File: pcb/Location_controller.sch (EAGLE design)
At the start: 55 parts, among them IC1 LIS302DL

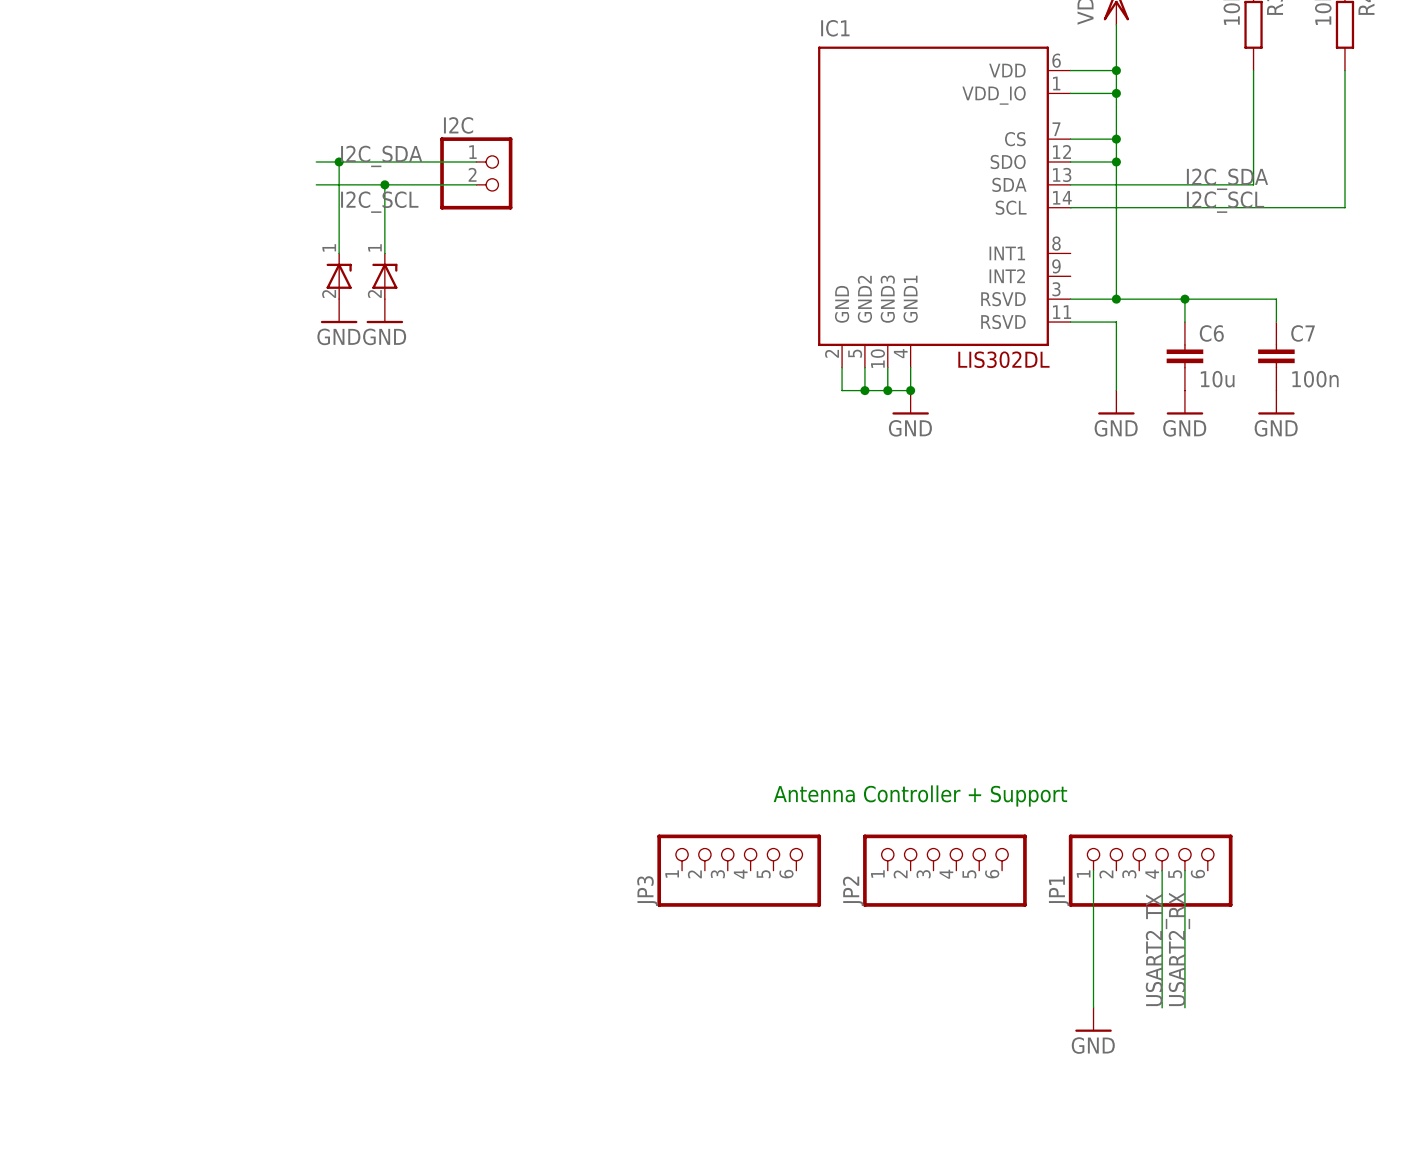
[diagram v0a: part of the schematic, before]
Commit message: Add TVS for I2C and USART connections
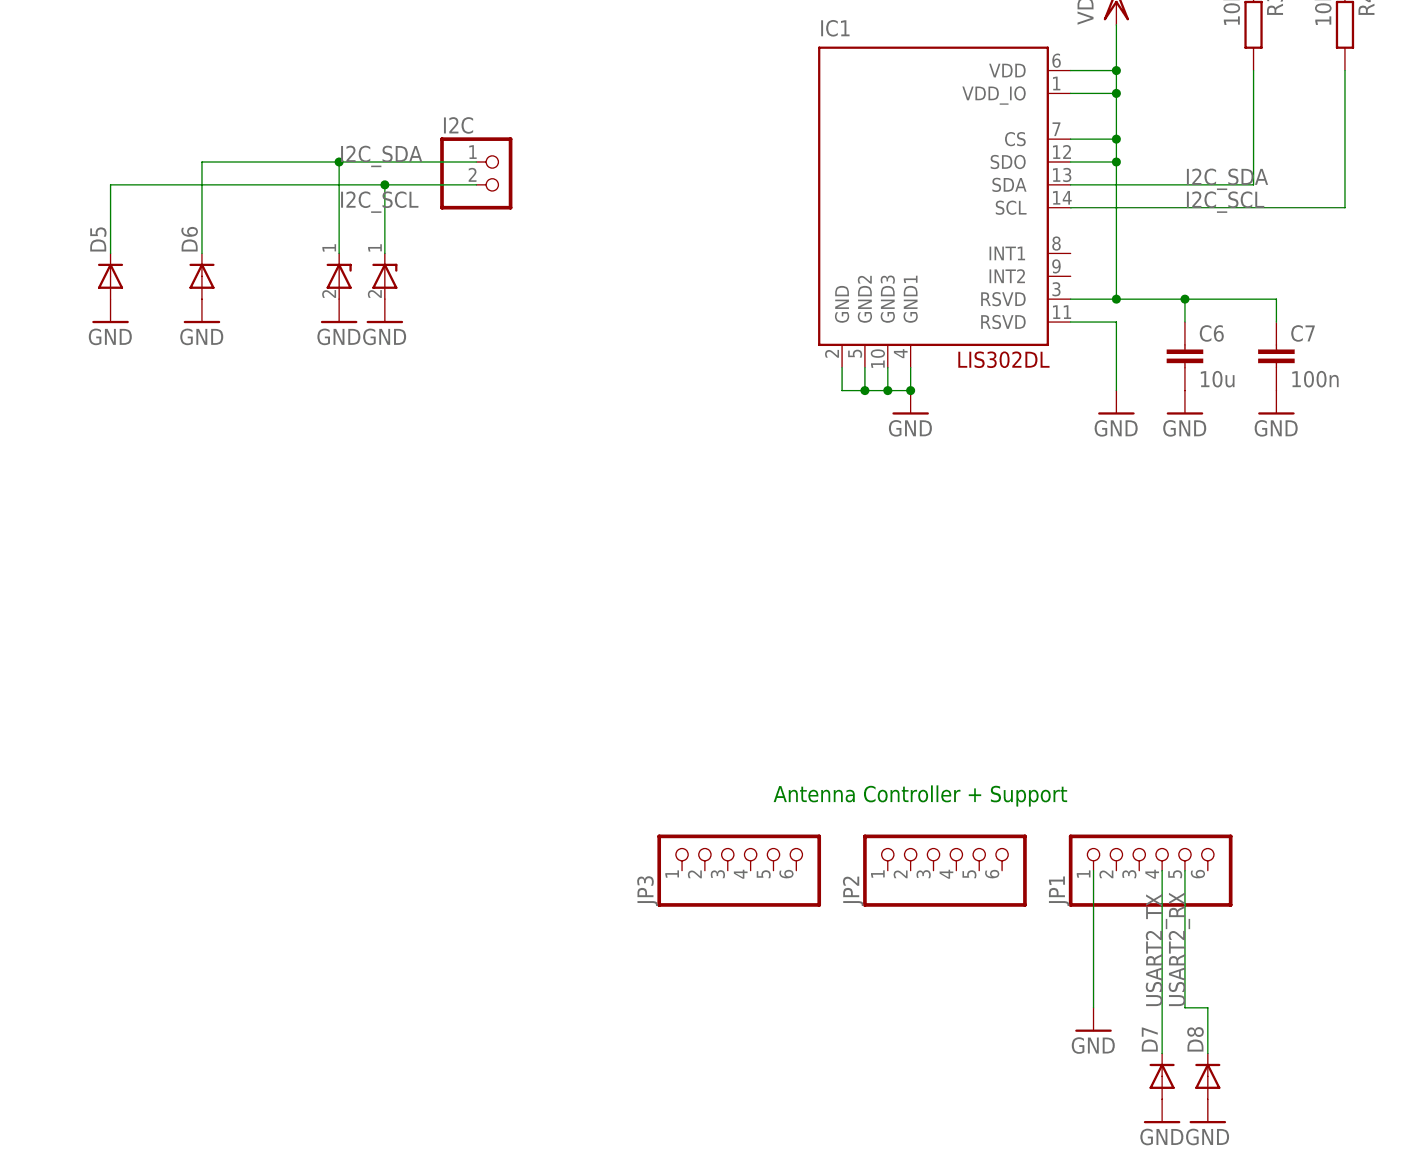
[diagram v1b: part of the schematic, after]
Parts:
- added D5, D6, D7, D8: (no value), diode:DIODE-SOD523
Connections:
- net GND: now also D5.A, D6.A, D7.A, D8.A
- net I2C_SCL: now also D5.C
- net I2C_SDA: now also D6.C
- net USART2_RX: now also D8.C
- net USART2_TX: now also D7.C
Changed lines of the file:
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@@
 <?xml version="1.0" encoding="utf-8"?>
 <!DOCTYPE eagle SYSTEM "eagle.dtd">
-<eagle version="6.4">
+<eagle version="6.5.0">
 <drawing>
 <settings>
@@
 <part name="D3" library="stm32f4" deviceset="ZDIODE" device=""/>
 <part name="GND25" library="supply1" deviceset="GND" device=""/>
+<part name="D5" library="diode" deviceset="DIODE-" device="SOD523"/>
+<part name="D6" library="diode" deviceset="DIODE-" device="SOD523"/>
+<part name="GND27" library="supply1" deviceset="GND" device=""/>
+<part name="GND28" library="supply1" deviceset="GND" device=""/>
+<part name="D7" library="diode" deviceset="DIODE-" device="SOD523"/>
+<part name="D8" library="diode" deviceset="DIODE-" device="SOD523"/>
+<part name="GND29" library="supply1" deviceset="GND" device=""/>
+<part name="GND30" library="supply1" deviceset="GND" device=""/>
 </parts>
 <sheets>
@@
 <instance part="D3" gate="G$1" x="78.74" y="-60.96" rot="R90"/>
 <instance part="GND25" gate="1" x="78.74" y="-88.9"/>
+<instance part="D5" gate="G$1" x="-149.86" y="2.54" rot="R90"/>
+<instance part="D6" gate="G$1" x="-139.7" y="2.54" rot="R90"/>
+<instance part="GND27" gate="1" x="-139.7" y="-2.54"/>
+<instance part="GND28" gate="1" x="-149.86" y="-2.54"/>
+<instance part="D7" gate="G$1" x="-33.02" y="-86.36" rot="R90"/>
+<instance part="D8" gate="G$1" x="-27.94" y="-86.36" rot="R90"/>
+<instance part="GND29" gate="1" x="-33.02" y="-91.44"/>
+<instance part="GND30" gate="1" x="-27.94" y="-91.44"/>
 </instances>
 <busses>
@@
 <wire x1="78.74" y1="-86.36" x2="78.74" y2="-63.5" width="0.1524" layer="91"/>
 </segment>
+<segment>
+<pinref part="D6" gate="G$1" pin="A"/>
+<pinref part="GND27" gate="1" pin="GND"/>
+</segment>
+<segment>
+<pinref part="D5" gate="G$1" pin="A"/>
+<pinref part="GND28" gate="1" pin="GND"/>
+</segment>
+<segment>
+<pinref part="D7" gate="G$1" pin="A"/>
+<pinref part="GND29" gate="1" pin="GND"/>
+</segment>
+<segment>
+<pinref part="D8" gate="G$1" pin="A"/>
+<pinref part="GND30" gate="1" pin="GND"/>
+</segment>
 </net>
 <net name="N$1" class="0">
@@
 <label x="-124.46" y="10.16" size="1.778" layer="95"/>
 <pinref part="D2" gate="G$1" pin="P1"/>
-<wire x1="-119.38" y1="12.7" x2="-127" y2="12.7" width="0.1524" layer="91"/>
 <wire x1="-119.38" y1="5.08" x2="-119.38" y2="12.7" width="0.1524" layer="91"/>
 <junction x="-119.38" y="12.7"/>
+<pinref part="D5" gate="G$1" pin="C"/>
+<wire x1="-119.38" y1="12.7" x2="-149.86" y2="12.7" width="0.1524" layer="91"/>
+<wire x1="-149.86" y1="12.7" x2="-149.86" y2="5.08" width="0.1524" layer="91"/>
 </segment>
 </net>
@@
 <label x="-124.46" y="15.24" size="1.778" layer="95"/>
 <pinref part="D1" gate="G$1" pin="P1"/>
-<wire x1="-124.46" y1="15.24" x2="-127" y2="15.24" width="0.1524" layer="91"/>
 <wire x1="-124.46" y1="5.08" x2="-124.46" y2="15.24" width="0.1524" layer="91"/>
 <junction x="-124.46" y="15.24"/>
+<pinref part="D6" gate="G$1" pin="C"/>
+<wire x1="-124.46" y1="15.24" x2="-139.7" y2="15.24" width="0.1524" layer="91"/>
+<wire x1="-139.7" y1="15.24" x2="-139.7" y2="5.08" width="0.1524" layer="91"/>
 </segment>
 </net>
@@
 <segment>
 <pinref part="JP1" gate="A" pin="4"/>
-<wire x1="-33.02" y1="-63.5" x2="-33.02" y2="-78.74" width="0.1524" layer="91"/>
+<wire x1="-33.02" y1="-63.5" x2="-33.02" y2="-83.82" width="0.1524" layer="91"/>
 <label x="-33.02" y="-78.74" size="1.778" layer="95" rot="R90"/>
+<pinref part="D7" gate="G$1" pin="C"/>
 </segment>
 </net>
@@
 <wire x1="-30.48" y1="-63.5" x2="-30.48" y2="-78.74" width="0.1524" layer="91"/>
 <label x="-30.48" y="-78.74" size="1.778" layer="95" rot="R90"/>
-</segment>
-</net>
+<pinref part="D8" gate="G$1" pin="C"/>
+<wire x1="-30.48" y1="-78.74" x2="-27.94" y2="-78.74" width="0.1524" layer="91"/>
+<wire x1="-27.94" y1="-78.74" x2="-27.94" y2="-83.82" width="0.1524" layer="91"/>
+</segment>
+</net>

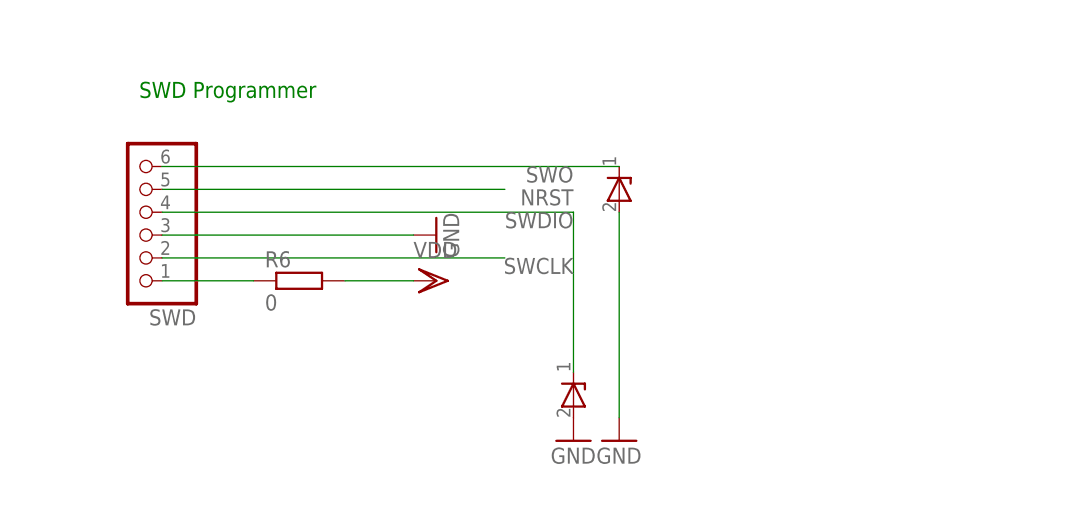
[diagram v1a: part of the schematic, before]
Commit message: Add TVS to programmer pins
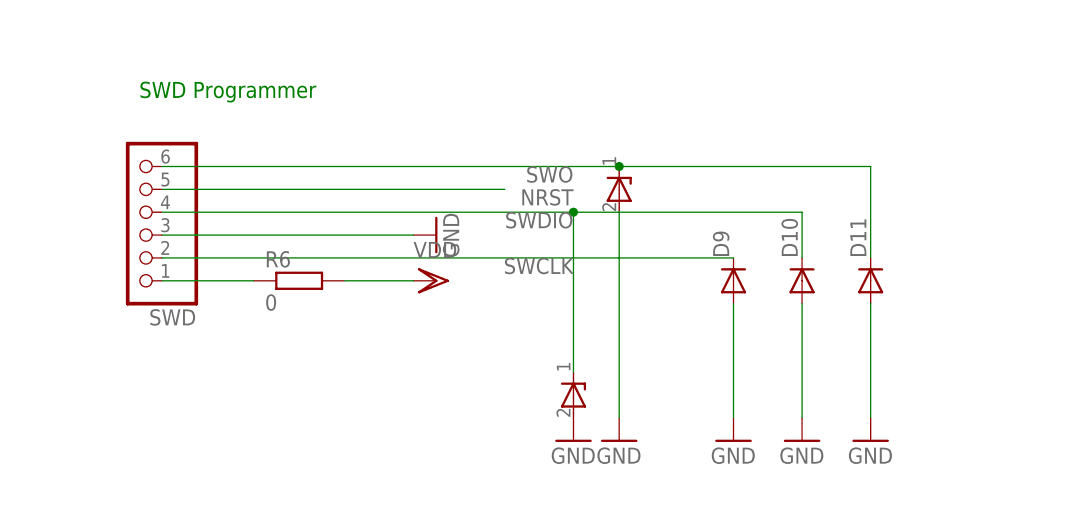
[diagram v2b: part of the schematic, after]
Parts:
- added D10, D11, D9: (no value), diode:DIODE-SOD523
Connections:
- net GND: now also D10.A, D11.A, D9.A
- net SWCLK: now also D9.C
- net SWDIO: now also D10.C
- net SWO: now also D11.C
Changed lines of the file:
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@@
 <part name="GND29" library="supply1" deviceset="GND" device=""/>
 <part name="GND30" library="supply1" deviceset="GND" device=""/>
+<part name="D9" library="diode" deviceset="DIODE-" device="SOD523"/>
+<part name="D10" library="diode" deviceset="DIODE-" device="SOD523"/>
+<part name="D11" library="diode" deviceset="DIODE-" device="SOD523"/>
+<part name="GND31" library="supply1" deviceset="GND" device=""/>
+<part name="GND32" library="supply1" deviceset="GND" device=""/>
+<part name="GND33" library="supply1" deviceset="GND" device=""/>
 </parts>
 <sheets>
@@
 <instance part="GND29" gate="1" x="-33.02" y="-91.44"/>
 <instance part="GND30" gate="1" x="-27.94" y="-91.44"/>
+<instance part="D9" gate="G$1" x="91.44" y="-71.12" rot="R90"/>
+<instance part="D10" gate="G$1" x="99.06" y="-71.12" rot="R90"/>
+<instance part="D11" gate="G$1" x="106.68" y="-71.12" rot="R90"/>
+<instance part="GND31" gate="1" x="91.44" y="-88.9"/>
+<instance part="GND32" gate="1" x="99.06" y="-88.9"/>
+<instance part="GND33" gate="1" x="106.68" y="-88.9"/>
 </instances>
 <busses>
@@
 <pinref part="GND30" gate="1" pin="GND"/>
 </segment>
+<segment>
+<pinref part="GND31" gate="1" pin="GND"/>
+<pinref part="D9" gate="G$1" pin="A"/>
+<wire x1="91.44" y1="-86.36" x2="91.44" y2="-73.66" width="0.1524" layer="91"/>
+</segment>
+<segment>
+<pinref part="D10" gate="G$1" pin="A"/>
+<pinref part="GND32" gate="1" pin="GND"/>
+<wire x1="99.06" y1="-73.66" x2="99.06" y2="-86.36" width="0.1524" layer="91"/>
+</segment>
+<segment>
+<pinref part="D11" gate="G$1" pin="A"/>
+<pinref part="GND33" gate="1" pin="GND"/>
+<wire x1="106.68" y1="-73.66" x2="106.68" y2="-86.36" width="0.1524" layer="91"/>
+</segment>
 </net>
 <net name="N$1" class="0">
@@
 <segment>
 <pinref part="SWD" gate="A" pin="2"/>
-<wire x1="27.94" y1="-68.58" x2="66.04" y2="-68.58" width="0.1524" layer="91"/>
+<wire x1="27.94" y1="-68.58" x2="91.44" y2="-68.58" width="0.1524" layer="91"/>
 <label x="73.66" y="-68.58" size="1.778" layer="95" rot="R180"/>
+<pinref part="D9" gate="G$1" pin="C"/>
 </segment>
 <segment>
@@
 <label x="73.66" y="-58.42" size="1.778" layer="95" rot="R180"/>
 <pinref part="D3" gate="G$1" pin="P1"/>
+<pinref part="D11" gate="G$1" pin="C"/>
+<wire x1="106.68" y1="-68.58" x2="106.68" y2="-58.42" width="0.1524" layer="91"/>
+<wire x1="106.68" y1="-58.42" x2="78.74" y2="-58.42" width="0.1524" layer="91"/>
+<junction x="78.74" y="-58.42"/>
 </segment>
 <segment>
@@
 <wire x1="73.66" y1="-63.5" x2="73.66" y2="-81.28" width="0.1524" layer="91"/>
 <pinref part="D4" gate="G$1" pin="P1"/>
-</segment>
-</net>
+<pinref part="D10" gate="G$1" pin="C"/>
+<wire x1="99.06" y1="-68.58" x2="99.06" y2="-63.5" width="0.1524" layer="91"/>
+<wire x1="99.06" y1="-63.5" x2="73.66" y2="-63.5" width="0.1524" layer="91"/>
+<junction x="73.66" y="-63.5"/>
+</segment>
+</net>

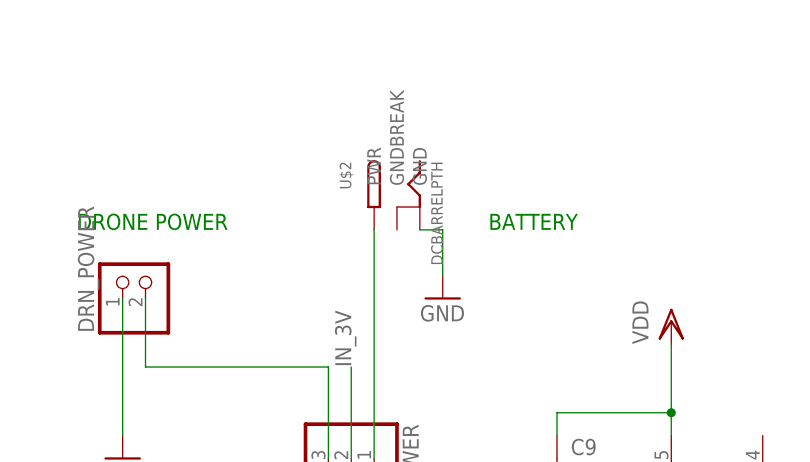
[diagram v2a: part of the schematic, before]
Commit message: Swap power plug for correct dimensions
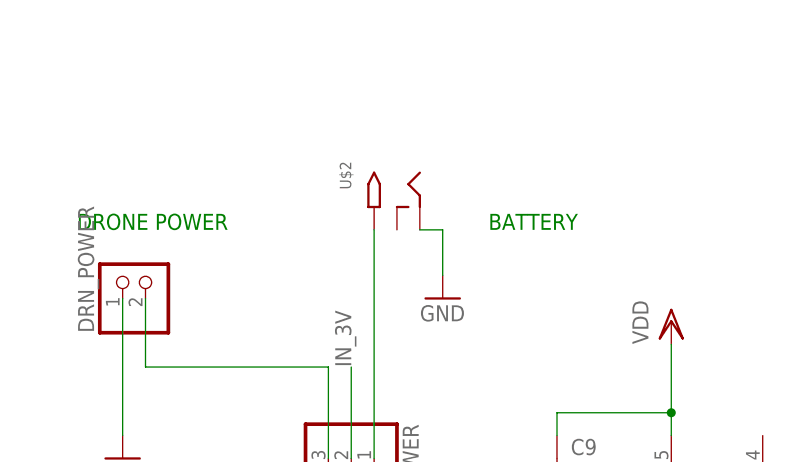
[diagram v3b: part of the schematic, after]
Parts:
- U$2: value DCBARRELPTH -> 2.1MMJACKTHM; device BaseApp:DCBARRELPTH -> adafruit:2.1MMJACKTHM
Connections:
- net GND: now also U$2.RING; no longer U$2.GND
- net N$5: now also U$2.TIP; no longer U$2.PWR
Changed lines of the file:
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@@
 <layer number="132" name="bAdjust" color="7" fill="1" visible="yes" active="yes"/>
 <layer number="144" name="Drill_legend" color="7" fill="1" visible="yes" active="yes"/>
+<layer number="150" name="Notes" color="7" fill="1" visible="no" active="yes"/>
 <layer number="151" name="HeatSink" color="7" fill="1" visible="yes" active="yes"/>
 <layer number="152" name="_bDocu" color="7" fill="1" visible="yes" active="yes"/>
+<layer number="153" name="FabDoc1" color="6" fill="1" visible="no" active="no"/>
+<layer number="154" name="FabDoc2" color="2" fill="1" visible="no" active="no"/>
+<layer number="155" name="FabDoc3" color="7" fill="15" visible="no" active="no"/>
 <layer number="199" name="Contour" color="7" fill="1" visible="yes" active="yes"/>
 <layer number="200" name="200bmp" color="1" fill="10" visible="no" active="no"/>
@@
 <part name="RCM_POWER" library="pinhead" deviceset="PINHD-1X2" device=""/>
 <part name="GND19" library="supply1" deviceset="GND" device=""/>
-<part name="U$2" library="BaseApp" deviceset="DCBARREL" device="PTH"/>
+<part name="U$2" library="adafruit" deviceset="2.1MMJACK" device="THM"/>
 <part name="JP1" library="pinhead" deviceset="PINHD-1X6" device=""/>
 <part name="JP2" library="pinhead" deviceset="PINHD-1X6" device=""/>
@@
 </segment>
 <segment>
-<pinref part="U$2" gate="G$1" pin="GND"/>
+<pinref part="U$2" gate="G$1" pin="RING"/>
 <pinref part="GND14" gate="1" pin="GND"/>
 <wire x1="-71.12" y1="127" x2="-68.58" y2="127" width="0.1524" layer="91"/>
@@
 <pinref part="POWER" gate="A" pin="1"/>
 <wire x1="-76.2" y1="127" x2="-76.2" y2="101.6" width="0.1524" layer="91"/>
-<pinref part="U$2" gate="G$1" pin="PWR"/>
-</segment>
-</net>
+<pinref part="U$2" gate="G$1" pin="TIP"/>
+</segment>
+</net>
